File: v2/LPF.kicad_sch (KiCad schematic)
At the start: 11 parts, among them U14 TLV9061xDBV

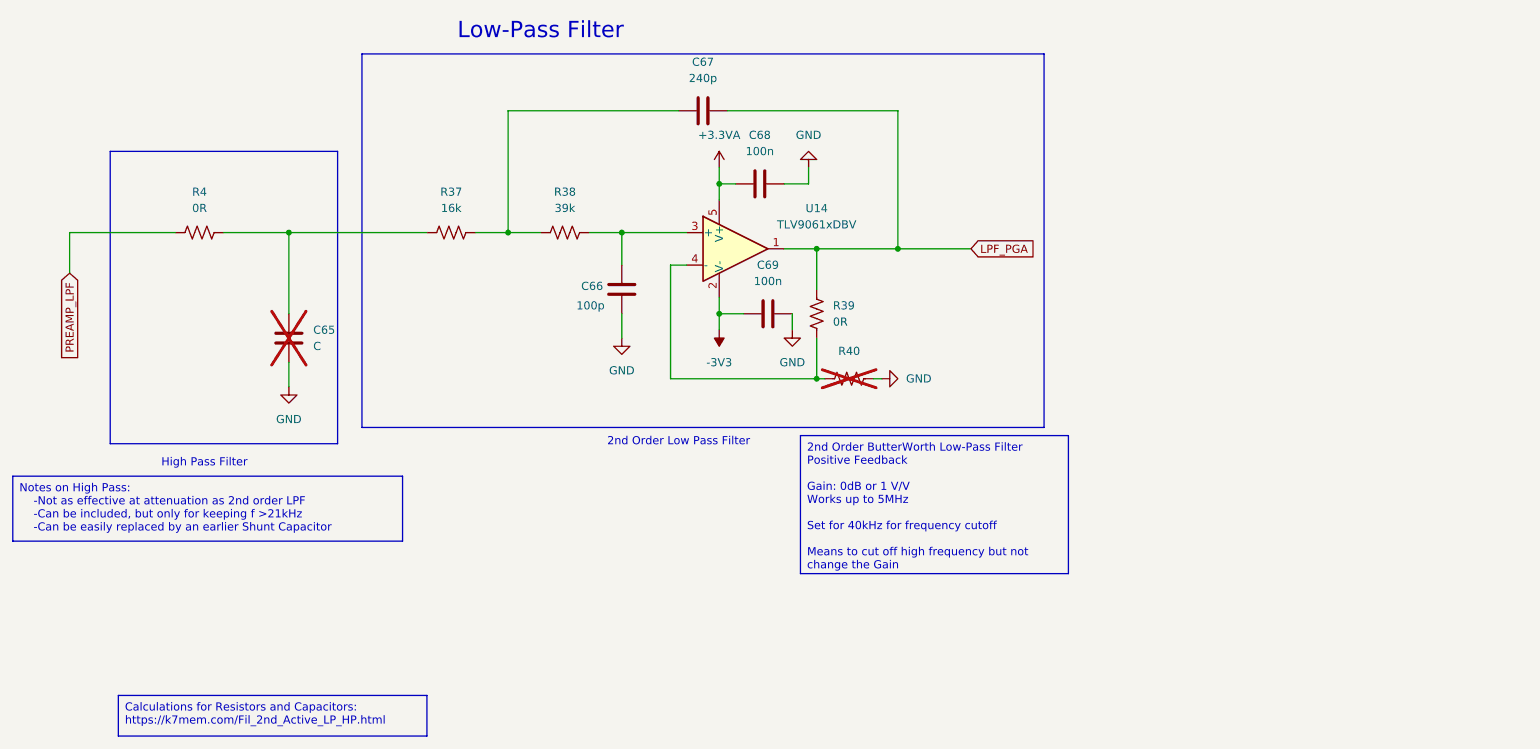
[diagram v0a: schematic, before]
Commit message: Most v2 changes made
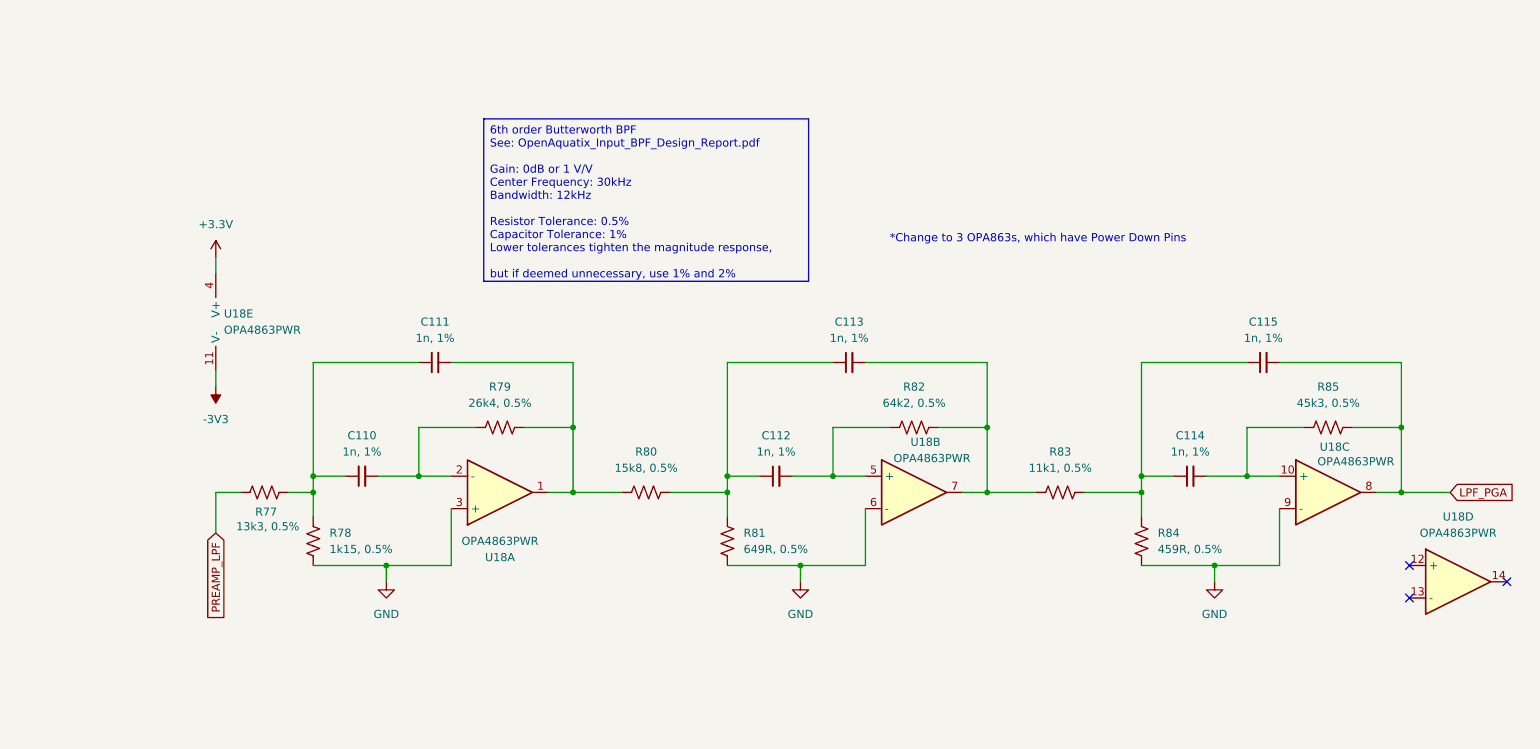
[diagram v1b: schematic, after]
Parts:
- removed C65: C, Capacitor_SMD:C_0603_1608Metric_Pad1.08x0.95mm_HandSolder, symbol UAM_symbols:C
- removed C66: 100p, Capacitor_SMD:C_0603_1608Metric_Pad1.08x0.95mm_HandSolder, symbol UAM_symbols:C
- removed C67: 240p, Capacitor_SMD:C_0603_1608Metric_Pad1.08x0.95mm_HandSolder, symbol UAM_symbols:C
- removed C68, C69: 100n, Capacitor_SMD:C_0603_1608Metric_Pad1.08x0.95mm_HandSolder, symbol UAM_symbols:C
- removed R37: 16k, Resistor_SMD:R_0603_1608Metric_Pad0.98x0.95mm_HandSolder, symbol UAM_symbols:R_US
- removed R38: 39k, Resistor_SMD:R_0603_1608Metric_Pad0.98x0.95mm_HandSolder, symbol UAM_symbols:R_US
- removed R39, R4: 0R, Resistor_SMD:R_0603_1608Metric_Pad0.98x0.95mm_HandSolder, symbol UAM_symbols:R_US
- removed R40: ~, Resistor_SMD:R_0603_1608Metric_Pad0.98x0.95mm_HandSolder, symbol UAM_symbols:R_US
- removed U14: TLV9061xDBV, Package_TO_SOT_SMD:SOT-23-5, symbol UAM_symbols:TLV9061xDBV
- added C110, C111, C112, C113, C114, C115: 1n, 1%, symbol Device:C_Small
- added R77: 13k3, 0.5%, symbol Device:R_US
- added R78: 1k15, 0.5%, symbol Device:R_US
- added R79: 26k4, 0.5%, symbol Device:R_US
- added R80: 15k8, 0.5%, symbol Device:R_US
- added R81: 649R, 0.5%, symbol Device:R_US
- added R82: 64k2, 0.5%, symbol Device:R_US
- added R83: 11k1, 0.5%, symbol Device:R_US
- added R84: 459R, 0.5%, symbol Device:R_US
- added R85: 45k3, 0.5%, symbol Device:R_US
- added U18: OPA4863PWR, UAM_footprints:SOP65P640X120-14N, symbol Device:Opamp_Quad
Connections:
- net -3V3: now also U18.11 (V-)
- net GND: now also R78.1, R81.1, R84.1, U18.3 (+), U18.6 (-), U18.9 (-)
- net LPF_PGA: now also C115.2, R85.1, U18.8
- net PREAMP_LPF: now also R77.1
- new net: C114.1, C115.1, R83.2, R84.2
- new net: C114.2, R85.2, U18.10 (+)
- new net: C110.1, C111.1, R77.2, R78.2
- new net: C111.2, R79.1, R80.1, U18.1
- new net: C113.2, R82.1, R83.1, U18.7
- new net: C110.2, R79.2, U18.2 (-)
- new net: C112.1, C113.1, R80.2, R81.2
- new net: C112.2, R82.2, U18.5 (+)
- new net +3.3V: U18.4 (V+)
- no-connect marks 0 -> 3
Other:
- note added: "*Change to 3 OPA863s, which have Power Down Pins"
- note removed: "2nd Order Low Pass Filter"
- note removed: "High Pass Filter"
- note removed: "Low-Pass Filter"
- company: RM -> (none)
- title: Low-Pass Filter -> (none)
